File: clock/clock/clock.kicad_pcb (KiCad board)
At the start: 2 copper layers, 32.3 x 110 mm, 44 parts, among them J1 AVR-ISP-6, J10 Conn_01x07_Male, J11 CV_IN, J12 CLOCK_OUT, J13 SUBDIV_OUT, J2 EURORACK_CONN_10, J3 Conn_01x05_Female, J4 Conn_01x05_Male, J5 Conn_01x05_Female, J6 Conn_01x05_Male, J7 Conn_01x05_Female, J8 Conn_01x05_Male, J9 Conn_01x07_Female, SW1 SW_Push, SW2 SW_Push, SW3 Rotary_Encoder_Switch, U1 ATmega328P-PU, U2 L7805, U3 SM460281N, U4 SM460281N, U5 SM460281N, Y1 16MHz

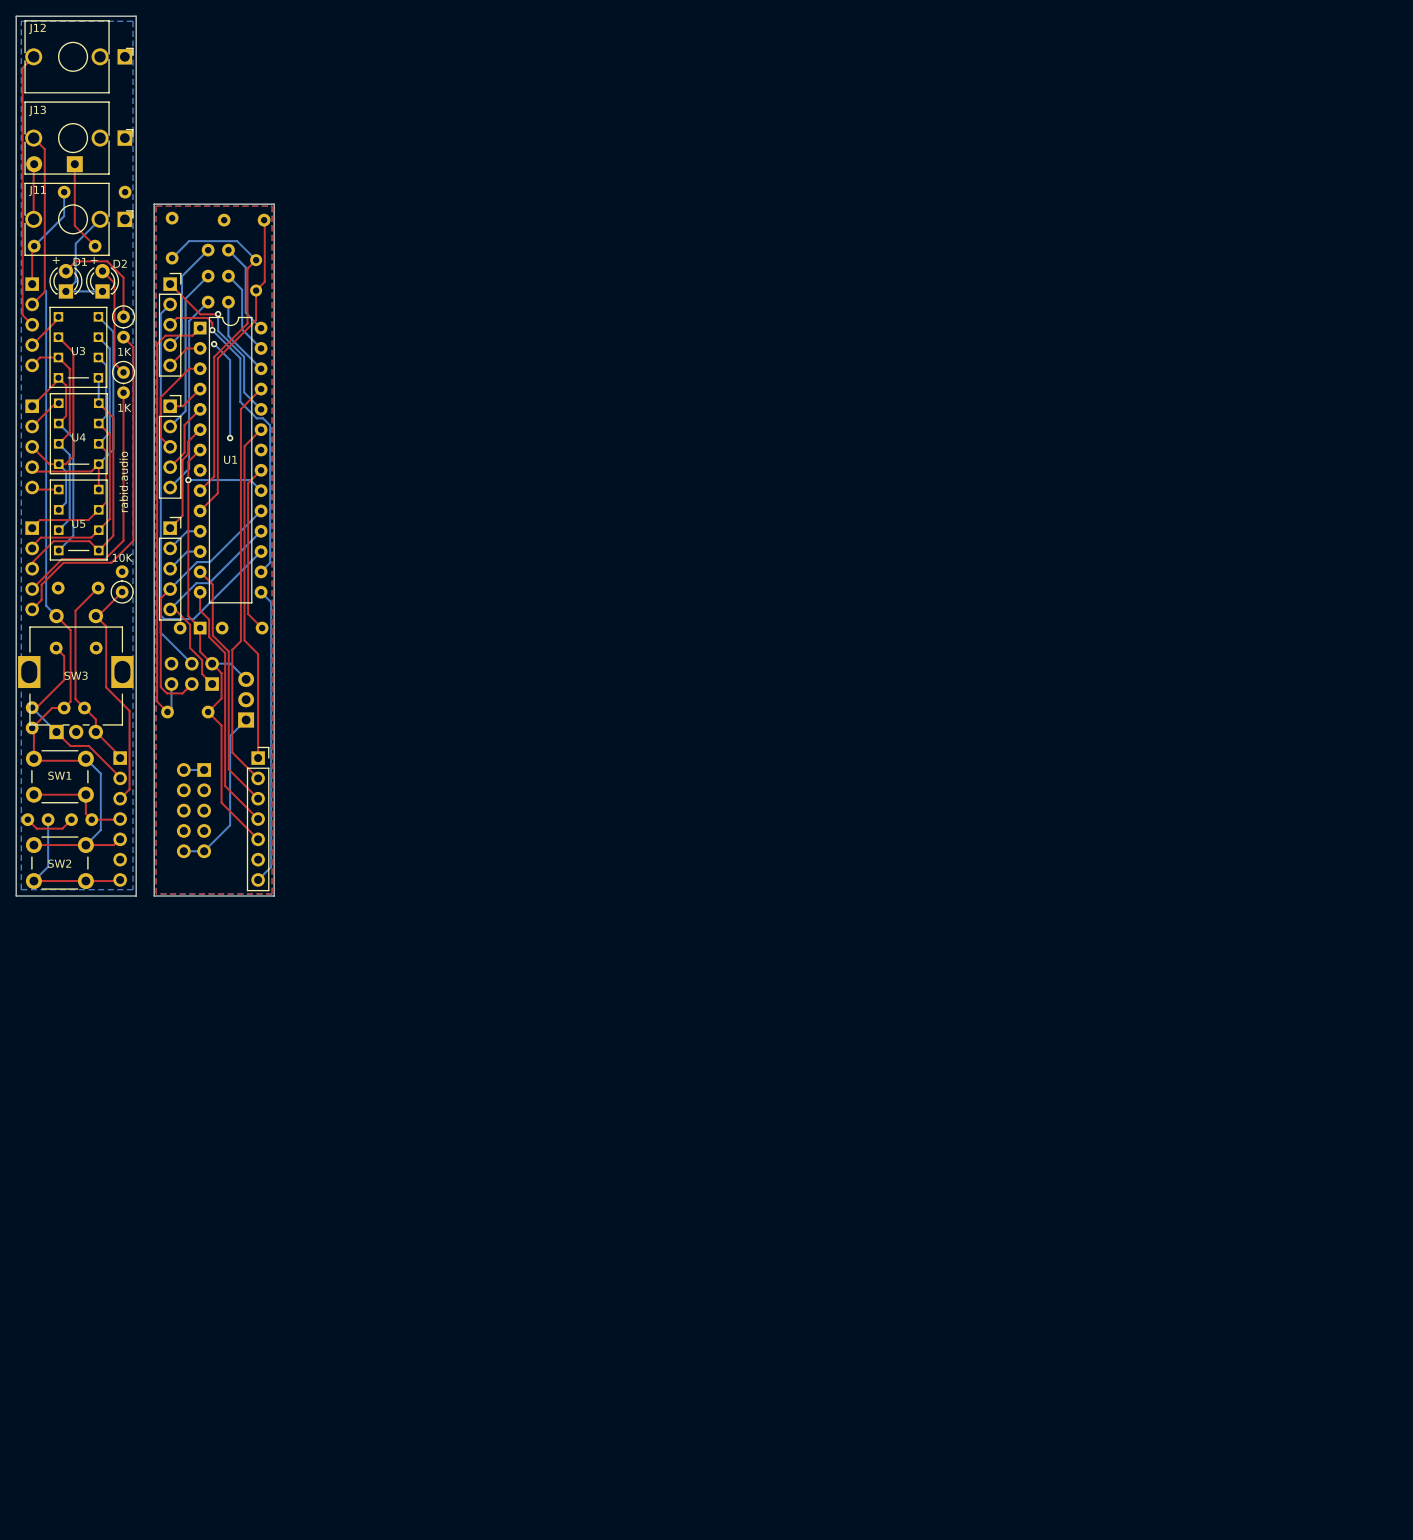
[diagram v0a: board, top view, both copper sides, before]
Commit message: update to Kicad 6 and fix some layout issues
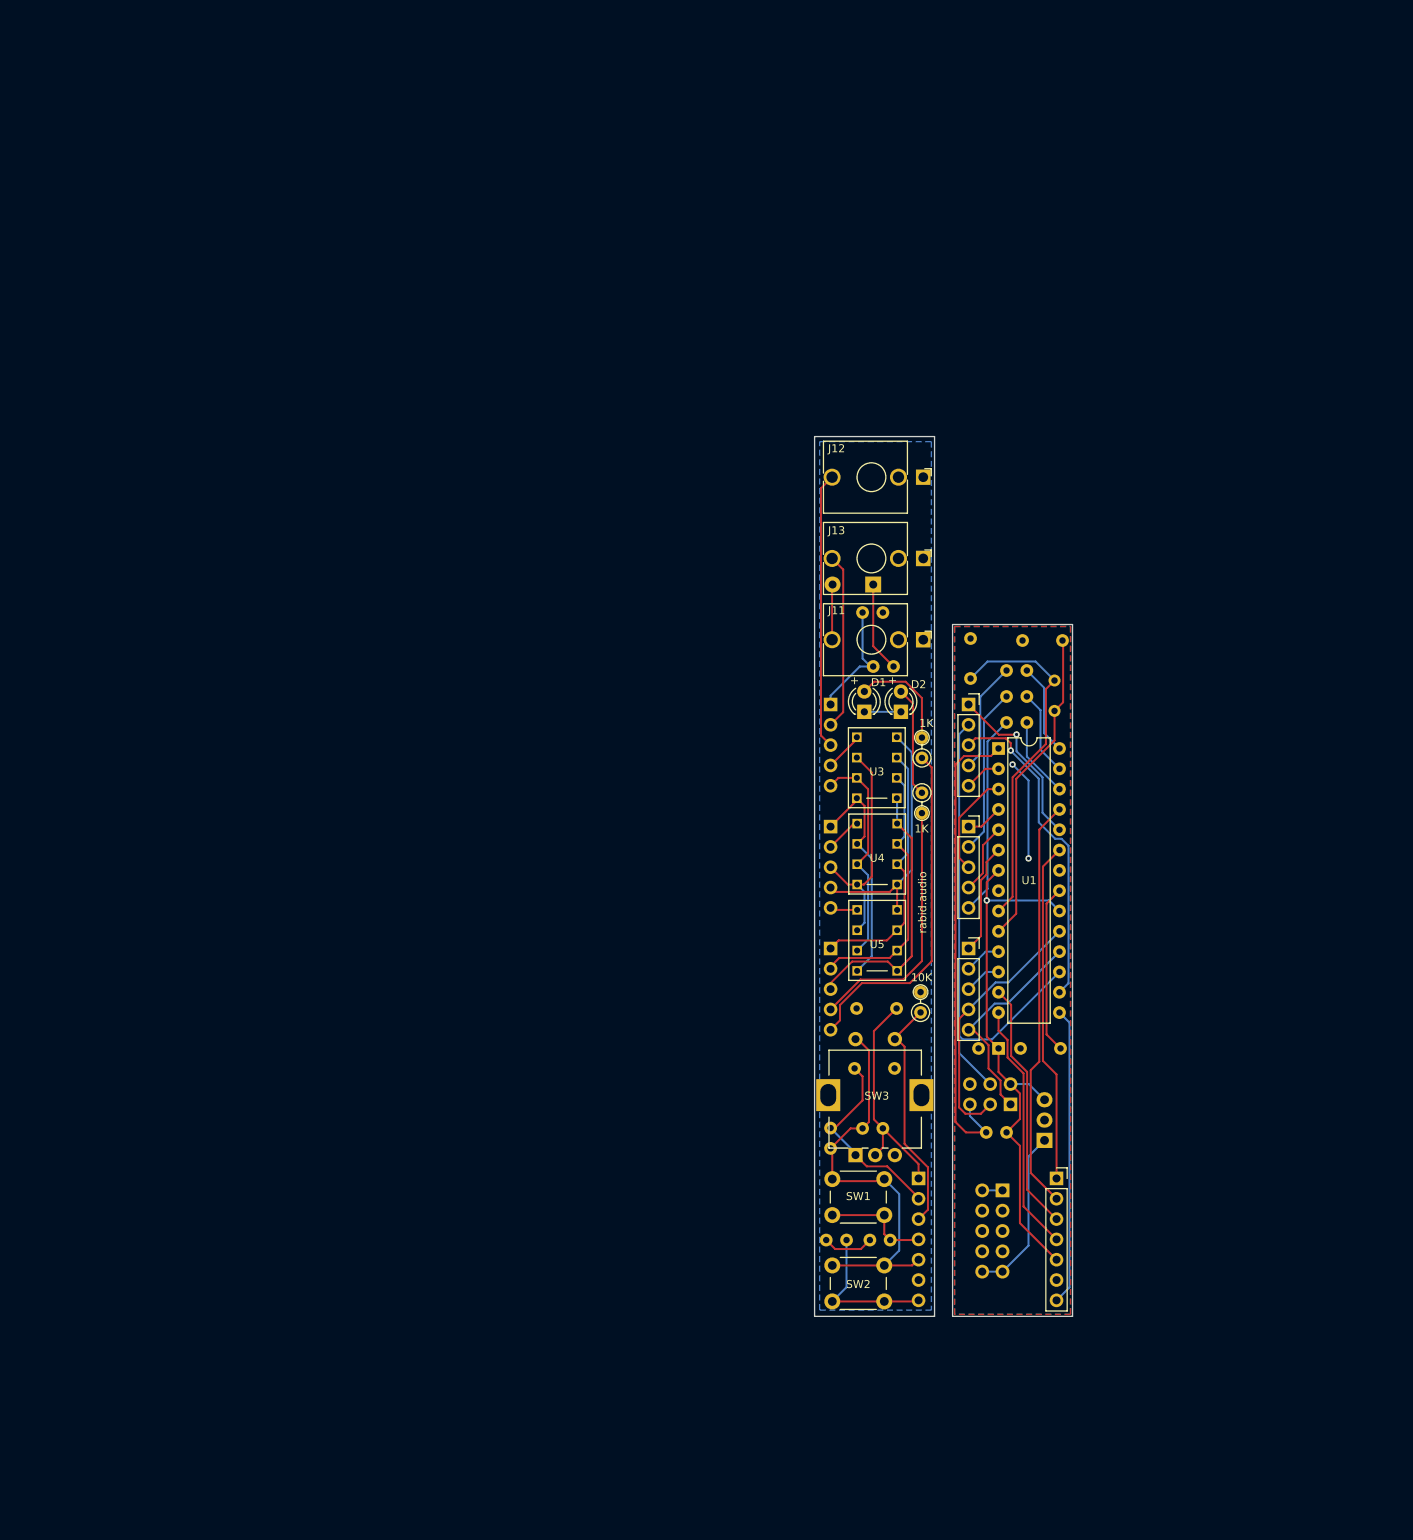
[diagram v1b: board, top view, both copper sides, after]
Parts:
- J1: value AVR-ISP-6 -> AVR-ISP
- R1: footprint Resistor_THT:R_Axial_DIN0207_L6.3mm_D2.5mm_P5.08mm_Vertical -> synth:R_Axial_DIN0207_L6.3mm_D2.5mm_P2.54mm_Vertical
- R10, R11, R13, R2, R3, R4, R5, R6, R7, R8: footprint Resistor_THT:R_Axial_DIN0207_L6.3mm_D2.5mm_P2.54mm_Vertical -> synth:R_Axial_DIN0207_L6.3mm_D2.5mm_P2.54mm_Vertical
- R14, R15: footprint Resistor_THT:R_Axial_DIN0207_L6.3mm_D2.5mm_P7.62mm_Horizontal -> synth:R_Axial_DIN0207_L6.3mm_D2.5mm_P2.54mm_Vertical
- moved R2 114.0 mm to (113.2, 92.7), turned to 90 degrees
- moved SW3 113.0 mm to (109.9, 142.4)
- moved C1 112.8 mm to (122.8, 129.1)
- moved C2 112.8 mm to (125.6, 129.1)
- moved C3 112.8 mm to (119.3, 77.8)
- moved C4 112.8 mm to (125.8, 78.1)
- moved C5 112.8 mm to (104.8, 131.6)
- moved C6 112.8 mm to (110.1, 124.1)
- moved D1 112.8 mm to (106.0, 87.0)
- moved D2 112.8 mm to (110.6, 87.0)
- moved D3 112.8 mm to (107.2, 71.1)
- moved J1 112.8 mm to (124.3, 136.1)
- moved J10 112.8 mm to (112.8, 145.3)
- moved J11 112.8 mm to (113.4, 78.0)
- moved J12 112.8 mm to (113.4, 57.6)
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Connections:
- net /~RESET renamed /~{RESET}
- J12 pad TN: Net-(J12-PadTN) -> unconnected-(J12-PadTN)
- J13 pad TN: Net-(J13-PadTN) -> unconnected-(J13-PadTN)
- J2 pad 1: Net-(J2-Pad1) -> unconnected-(J2-Pad1)
- R2 pad 1: Net-(D1-Pad2) -> /LEDL
- R2 pad 2: /LEDL -> Net-(D1-Pad2)
- SW3 pad 2: /AGND -> /KNOBR
- SW3 pad 3: /KNOBR -> /AGND
- SW3 pad 4: /SW3 -> /AVCC
- SW3 pad 5: /AVCC -> /SW3
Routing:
- net /AVCC: track 92.7 -> 51.5 mm
- net /AGND: track 22.4 -> 11.0 mm
- net /~{RESET}: track 56.8 -> 59.6 mm
- net /KNOBR: track 25.9 -> 28.5 mm
- net unconnected-(J2-Pad1): track 0.00 -> 2.54 mm
- net Net-(J2-Pad1): track 2.54 -> 0.00 mm
- net /CV_IN: track 13.2 -> 14.8 mm
- net /B_LEDR: track 34.0 -> 32.9 mm
- net /B_LED6: track 5.64 -> 4.64 mm
- net /B_LED5: track 5.64 -> 4.64 mm
- net /B_CV_IN: track 22.4 -> 21.7 mm
- net /LEDR: track 33.1 -> 32.4 mm
- net /B_LED0: track 5.17 -> 4.63 mm
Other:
- net class Default removed
- board text added: "2023-01-01 REV. A"
- board text removed: "2022-11-24 REV. A"
